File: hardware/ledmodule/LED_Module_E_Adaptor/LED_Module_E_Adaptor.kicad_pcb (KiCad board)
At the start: 2 copper layers, 52.1 x 52.1 mm, 15 parts, among them J1 Conn_01x16_Socket, J2 Conn_01x16_Socket, J3 Conn_02x11_Odd_Even, J4 Conn_02x02_Odd_Even, J5 Screw_Terminal_01x02, J6 Conn_02x07_Odd_Even, J7 Grove I2C 3.3V, J8 Grove I2C 5V

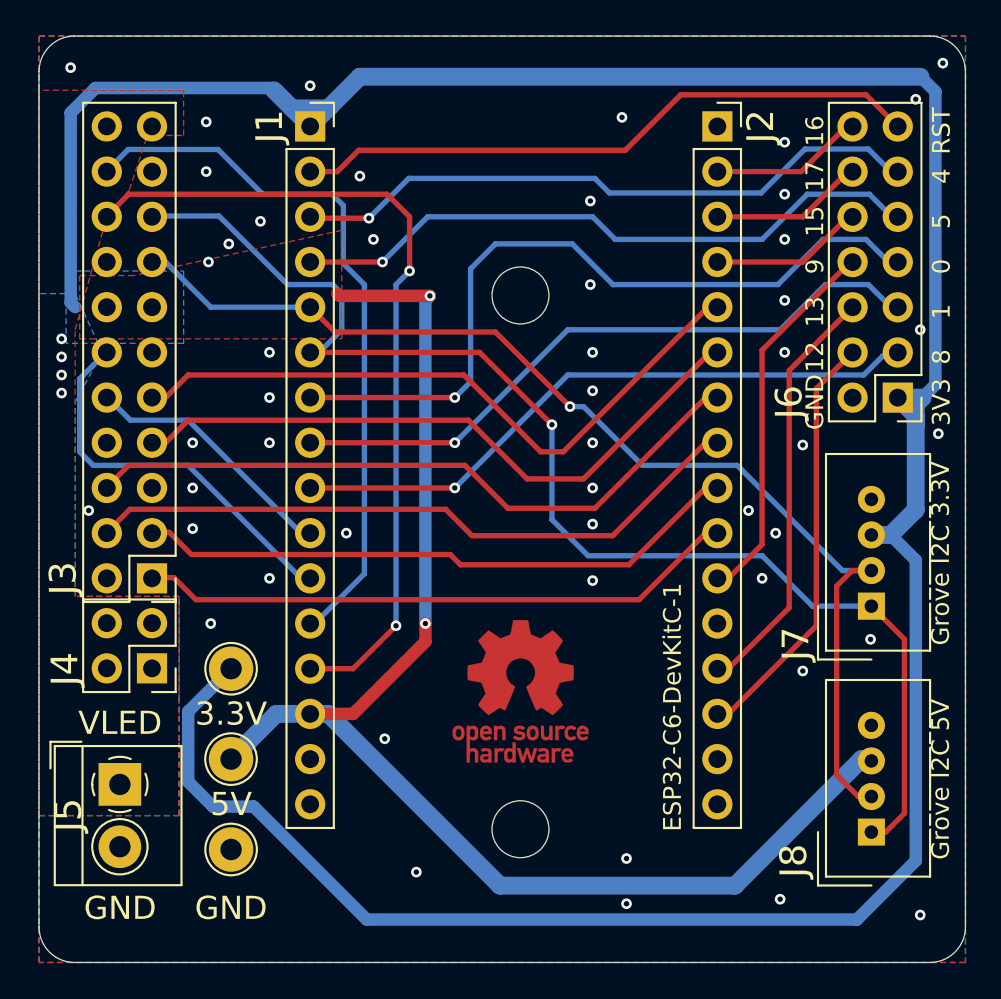
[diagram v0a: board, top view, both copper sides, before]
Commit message: Upgrade LED module E adaptor  to v1.1 with improved GND return path.
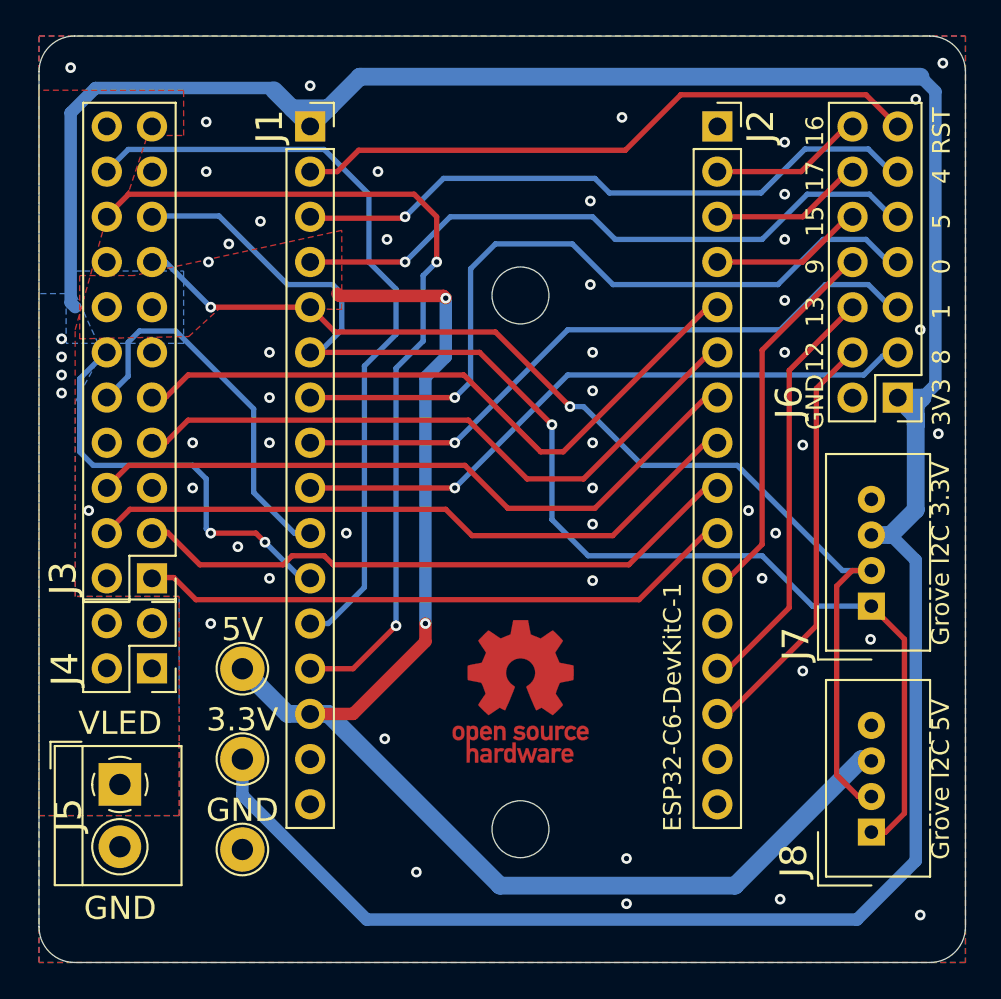
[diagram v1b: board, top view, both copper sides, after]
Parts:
- moved H5 5.12 mm to (39.4, 94.0)
- moved H4 5.12 mm to (39.4, 99.1)
- moved H1 0.63 mm to (39.4, 104.1)
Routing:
- net +3.3V: track 166.8 -> 158.1 mm
- net /LED_7: track 14.6 -> 21.6 mm
- net /ENABLE: track 40.5 -> 43.6 mm
- net /ALERT: track 47.2 -> 49.3 mm
- net /LED_8: track 22.6 -> 24.2 mm, vias 0 -> 2
- net +5V: track 77.3 -> 77.8 mm
- net /SDA: vias 1 -> 2
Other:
- board text added: "Adaptor for v1.1"
- board text removed: "Adaptor for v1.0"
